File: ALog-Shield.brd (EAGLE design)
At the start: 53.3 x 78.5 mm, 32 parts

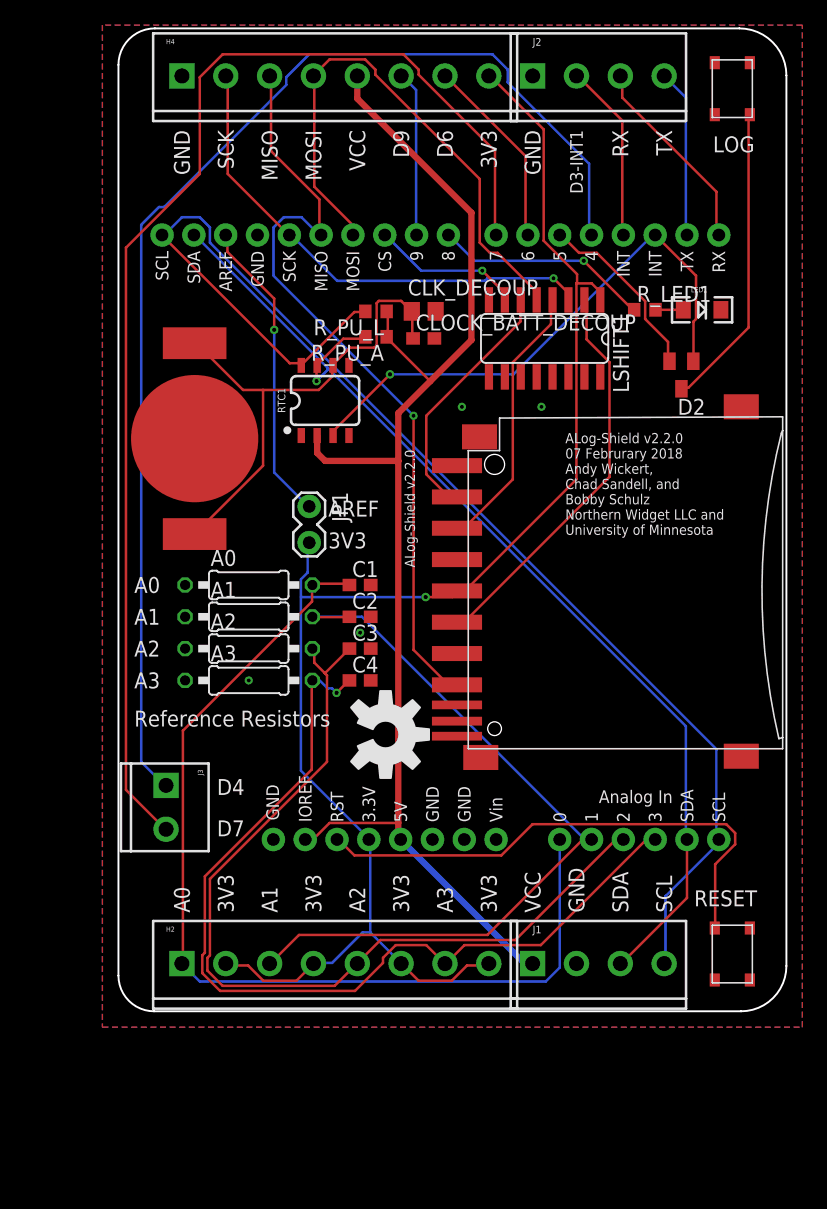
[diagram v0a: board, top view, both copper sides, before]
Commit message: IO Ref conversion
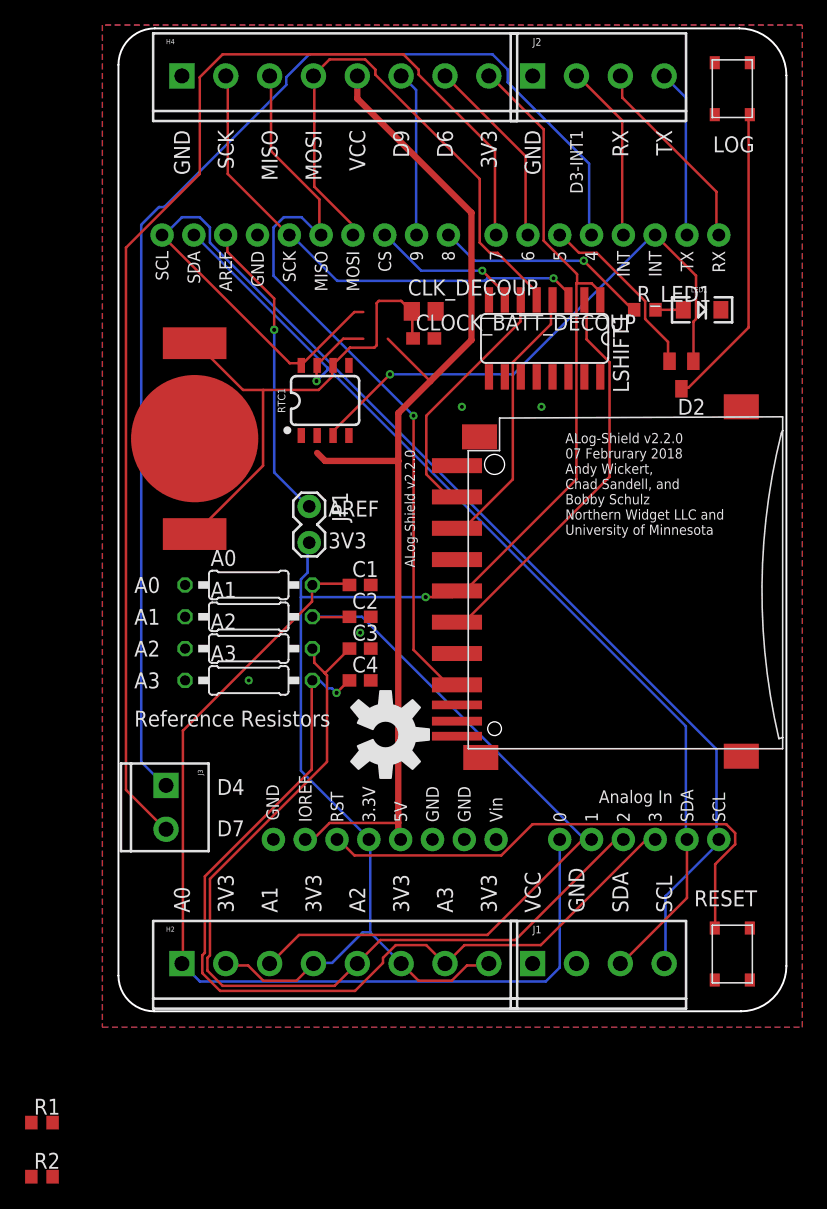
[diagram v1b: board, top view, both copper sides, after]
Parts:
- removed R_PU_A, R_PU_L: 10k, bschulz_passives:R0603
- added R1, R2: 10k, bschulz:R0603
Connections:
- new net 5V: U$9.5V
- net SCL: now also R1.1; no longer R_PU_L.2
- net SDA: now also R2.1; no longer R_PU_A.2
- net VCC: now also R1.2, R2.2; no longer R_PU_A.1, R_PU_L.1, U$9.5V
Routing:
- net VCC: track 105.4 -> 87.1 mm
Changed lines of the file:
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@@
 <?xml version="1.0" encoding="utf-8"?>
 <!DOCTYPE eagle SYSTEM "eagle.dtd">
-<eagle version="8.6.0">
+<eagle version="8.5.1">
 <drawing>
 <settings>
@@
 <layer number="20" name="Dimension" color="15" fill="1" visible="yes" active="yes"/>
 <layer number="21" name="tPlace" color="7" fill="1" visible="yes" active="yes"/>
-<layer number="22" name="bPlace" color="7" fill="1" visible="yes" active="yes"/>
+<layer number="22" name="bPlace" color="7" fill="1" visible="no" active="yes"/>
 <layer number="23" name="tOrigins" color="15" fill="1" visible="yes" active="yes"/>
 <layer number="24" name="bOrigins" color="15" fill="1" visible="yes" active="yes"/>
@@
 </element>
 <element name="JP1" library="SparkFun-Connectors" package="1X02_LOCK" value="" x="15.24" y="40.132" rot="R270"/>
-<element name="R_PU_L" library="bschulz_passives" package="R0603" value="10k" x="20.574" y="55.88" rot="R180">
-<attribute name="DIGIKEY" value="311-10.0KHRCT-ND" x="20.574" y="55.88" size="1.778" layer="27" rot="R180" display="off"/>
-<attribute name="MF" value="Yageo" x="20.574" y="55.88" size="1.778" layer="27" rot="R180" display="off"/>
-<attribute name="MPN" value="RC0603FR-0710KL" x="20.574" y="55.88" size="1.778" layer="27" rot="R180" display="off"/>
-<attribute name="VALUE_PART" value="10k" x="20.574" y="55.88" size="1.778" layer="27" rot="R180" display="off"/>
-</element>
-<element name="R_PU_A" library="bschulz_passives" package="R0603" value="10k" x="20.574" y="53.848" rot="R180">
-<attribute name="DIGIKEY" value="311-10.0KHRCT-ND" x="20.574" y="53.848" size="1.778" layer="27" rot="R180" display="off"/>
-<attribute name="MF" value="Yageo" x="20.574" y="53.848" size="1.778" layer="27" rot="R180" display="off"/>
-<attribute name="MPN" value="RC0603FR-0710KL" x="20.574" y="53.848" size="1.778" layer="27" rot="R180" display="off"/>
-<attribute name="VALUE_PART" value="10k" x="20.574" y="53.848" size="1.778" layer="27" rot="R180" display="off"/>
-</element>
 <element name="C1" library="bschulz_passives" package="C0603" value="" x="19.304" y="34.036">
 <attribute name="DIGIKEY" value="1276-1005-1-ND" x="19.304" y="34.036" size="1.778" layer="27" display="off"/>
@@
 <attribute name="MF" value="Maxim" x="16.51" y="48.768" size="1.778" layer="27" display="off"/>
 <attribute name="MPN" value="DS3231MZ+" x="16.51" y="48.768" size="1.778" layer="27" display="off"/>
+</element>
+<element name="R1" library="bschulz" package="R0603" value="10k" x="-6.096" y="-8.89">
+<attribute name="DIGIKEY" value="" x="-6.096" y="-8.89" size="1.778" layer="27" display="off"/>
+<attribute name="MF" value="" x="-6.096" y="-8.89" size="1.778" layer="27" display="off"/>
+<attribute name="MPN" value="" x="-6.096" y="-8.89" size="1.778" layer="27" display="off"/>
+<attribute name="VALUE_PART" value="" x="-6.096" y="-8.89" size="1.778" layer="27" display="off"/>
+</element>
+<element name="R2" library="bschulz" package="R0603" value="10k" x="-6.096" y="-13.208">
+<attribute name="DIGIKEY" value="" x="-6.096" y="-13.208" size="1.778" layer="27" display="off"/>
+<attribute name="MF" value="" x="-6.096" y="-13.208" size="1.778" layer="27" display="off"/>
+<attribute name="MPN" value="" x="-6.096" y="-13.208" size="1.778" layer="27" display="off"/>
+<attribute name="VALUE_PART" value="" x="-6.096" y="-13.208" size="1.778" layer="27" display="off"/>
 </element>
 </elements>
@@
 </signal>
 <signal name="VCC">
-<contactref element="U$9" pad="5V"/>
 <contactref element="J1" pad="1"/>
 <contactref element="H4" pad="5"/>
-<contactref element="U$9" pad="IOREF"/>
 <wire x1="19.08" y1="74.676" x2="19.08" y2="72.868" width="0.508" layer="1"/>
 <wire x1="19.08" y1="72.868" x2="28.194" y2="63.754" width="0.508" layer="1"/>
@@
 <wire x1="16.8656" y1="15.0368" x2="15.6464" y2="13.8176" width="0.2032" layer="1"/>
 <wire x1="22.352" y1="15.0368" x2="16.8656" y2="15.0368" width="0.2032" layer="1"/>
-<wire x1="15.0368" y1="13.8176" x2="14.9225" y2="13.716" width="0.2032" layer="1"/>
 <wire x1="22.352" y1="15.0368" x2="22.352" y2="13.9065" width="0.508" layer="1"/>
-<wire x1="22.352" y1="13.9065" x2="22.5425" y2="13.716" width="0.508" layer="1"/>
-<wire x1="22.5425" y1="13.716" x2="32.4485" y2="3.81" width="0.508" layer="16"/>
 <wire x1="32.4485" y1="3.81" x2="33.08" y2="3.81" width="0.508" layer="16"/>
-<contactref element="R_PU_L" pad="1"/>
-<contactref element="R_PU_A" pad="1"/>
-<wire x1="21.5138" y1="56.007" x2="21.424" y2="55.88" width="0.2032" layer="1"/>
+<wire x1="24.9047" y1="50.3047" x2="21.5138" y2="53.6956" width="0.2032" layer="1"/>
+<wire x1="16.51" y1="43.942" x2="15.875" y2="44.577" width="0.508" layer="1"/>
 <contactref element="RTC1" pad="2"/>
-<wire x1="21.5138" y1="55.8292" x2="21.5138" y2="53.8734" width="0.2032" layer="1"/>
-<wire x1="21.5138" y1="53.8734" x2="21.424" y2="53.848" width="0.2032" layer="1"/>
-<wire x1="21.5138" y1="55.8292" x2="21.424" y2="55.88" width="0.2032" layer="1"/>
-<wire x1="24.9047" y1="50.3047" x2="21.5138" y2="53.6956" width="0.2032" layer="1"/>
-<wire x1="21.5138" y1="53.6956" x2="21.424" y2="53.848" width="0.2032" layer="1"/>
 <wire x1="16.002" y1="45.8724" x2="15.875" y2="45.968" width="0.2032" layer="1"/>
-<wire x1="15.875" y1="44.577" x2="15.875" y2="45.968" width="0.508" layer="1"/>
-<wire x1="16.51" y1="43.942" x2="15.875" y2="44.577" width="0.508" layer="1"/>
+<contactref element="U$9" pad="IOREF"/>
+<contactref element="R1" pad="2"/>
+<contactref element="R2" pad="2"/>
+<wire x1="15.875" y1="44.577" x2="16.002" y2="45.8724" width="0" layer="19" extent="1-1"/>
+<wire x1="14.9225" y1="13.716" x2="15.0368" y2="13.8176" width="0" layer="19" extent="1-1"/>
+<wire x1="32.4485" y1="3.81" x2="22.352" y2="13.9065" width="0" layer="19" extent="1-16"/>
+<wire x1="-5.246" y1="-8.89" x2="14.9225" y2="13.716" width="0" layer="19" extent="1-1"/>
+<wire x1="-5.246" y1="-13.208" x2="-5.246" y2="-8.89" width="0" layer="19" extent="1-1"/>
 </signal>
 <signal name="DI">
@@
 <wire x1="47.752" y1="13.8176" x2="47.9425" y2="13.716" width="0.2032" layer="16"/>
 <wire x1="3.6576" y1="61.976" x2="3.4925" y2="61.976" width="0.2032" layer="16"/>
-<contactref element="R_PU_L" pad="2"/>
+<wire x1="13.6906" y1="51.7398" x2="14.5796" y2="51.7398" width="0.2032" layer="1"/>
+<wire x1="3.556" y1="61.8744" x2="13.6906" y2="51.7398" width="0.2032" layer="1"/>
+<wire x1="3.556" y1="61.8744" x2="3.4925" y2="61.976" width="0.2032" layer="1"/>
 <contactref element="RTC1" pad="8"/>
 <wire x1="18.8468" y1="55.8292" x2="19.558" y2="55.8292" width="0.2032" layer="1"/>
 <wire x1="14.7574" y1="51.7398" x2="18.8468" y2="55.8292" width="0.2032" layer="1"/>
-<wire x1="19.558" y1="55.8292" x2="19.724" y2="55.88" width="0.2032" layer="1"/>
 <wire x1="14.7574" y1="51.7398" x2="14.605" y2="51.568" width="0.2032" layer="1"/>
-<wire x1="13.6906" y1="51.7398" x2="14.5796" y2="51.7398" width="0.2032" layer="1"/>
-<wire x1="3.556" y1="61.8744" x2="13.6906" y2="51.7398" width="0.2032" layer="1"/>
-<wire x1="14.5796" y1="51.7398" x2="14.605" y2="51.568" width="0.2032" layer="1"/>
-<wire x1="3.556" y1="61.8744" x2="3.4925" y2="61.976" width="0.2032" layer="1"/>
+<contactref element="R1" pad="1"/>
+<wire x1="14.5796" y1="51.7398" x2="14.7574" y2="51.7398" width="0" layer="19" extent="1-1"/>
+<wire x1="-6.946" y1="-8.89" x2="43.58" y2="3.81" width="0" layer="19" extent="1-1"/>
 </signal>
 <signal name="SDA">
@@
 <wire x1="45.3136" y1="13.8176" x2="45.4025" y2="13.716" width="0.2032" layer="16"/>
 <wire x1="6.096" y1="61.976" x2="6.0325" y2="61.976" width="0.2032" layer="16"/>
-<contactref element="R_PU_A" pad="2"/>
+<wire x1="15.8242" y1="50.3174" x2="15.8242" y2="51.562" width="0.2032" layer="1"/>
+<wire x1="16.7132" y1="51.2064" x2="15.8242" y2="50.3174" width="0.2032" layer="16"/>
+<wire x1="16.7132" y1="51.3842" x2="16.7132" y2="51.2064" width="0.2032" layer="16"/>
+<wire x1="16.7132" y1="51.3842" x2="16.7005" y2="51.3715" width="0.2032" layer="16"/>
+<via x="15.8242" y="50.3174" extent="1-16" drill="0.3302"/>
 <contactref element="RTC1" pad="7"/>
 <wire x1="17.9578" y1="53.6956" x2="19.558" y2="53.6956" width="0.2032" layer="1"/>
 <wire x1="16.002" y1="51.7398" x2="17.9578" y2="53.6956" width="0.2032" layer="1"/>
-<wire x1="19.558" y1="53.6956" x2="19.724" y2="53.848" width="0.2032" layer="1"/>
 <wire x1="16.002" y1="51.7398" x2="15.875" y2="51.568" width="0.2032" layer="1"/>
-<wire x1="15.8242" y1="50.3174" x2="15.8242" y2="51.562" width="0.2032" layer="1"/>
-<wire x1="16.7132" y1="51.2064" x2="15.8242" y2="50.3174" width="0.2032" layer="16"/>
-<wire x1="16.7132" y1="51.3842" x2="16.7132" y2="51.2064" width="0.2032" layer="16"/>
-<wire x1="15.8242" y1="51.562" x2="15.875" y2="51.568" width="0.2032" layer="1"/>
-<wire x1="16.7132" y1="51.3842" x2="16.7005" y2="51.3715" width="0.2032" layer="16"/>
-<via x="15.8242" y="50.3174" extent="1-16" drill="0.3302"/>
+<contactref element="R2" pad="1"/>
+<wire x1="15.8242" y1="51.562" x2="15.875" y2="51.568" width="0" layer="19" extent="1-1"/>
+<wire x1="-6.946" y1="-13.208" x2="40.08" y2="3.81" width="0" layer="19" extent="1-1"/>
 </signal>
 <signal name="INT0">
@@
 <via x="12.446" y="54.4068" extent="1-16" drill="0.3302"/>
 </signal>
+<signal name="5V">
+<contactref element="U$9" pad="5V"/>
+</signal>
 </signals>

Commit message: PU, reroute, 5V terminal
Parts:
- removed J3: (no value), SparkFun-Connectors:SCREWTERMINAL-3.5MM-2
- added JP2: (no value), SparkFun-Connectors:SCREWTERMINAL-3.5MM-3
- moved R2 71.8 mm to (19.6, 53.8), turned to 180 degrees
- moved R1 69.7 mm to (19.6, 55.9)
- moved CLK_DECOUP 0.57 mm to (23.9, 56.1)
- moved CLOCK_BATT_DECOUP 0.51 mm to (23.9, 53.7)
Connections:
- net 5V: now also JP2.3
- net D4: now also JP2.1; no longer J3.1
- net D7: now also JP2.2; no longer J3.2
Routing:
- net VCC: track 87.1 -> 114.7 mm, vias 0 -> 1
- net 5V: track 0.00 -> 20.5 mm, vias 0 -> 1
- net D4: track 97.5 -> 85.0 mm
- net D7: track 98.4 -> 91.6 mm
- net BAT: track 40.8 -> 37.4 mm
- net SDA: track 84.0 -> 85.0 mm
- net SCL: track 104.3 -> 103.4 mm
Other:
- board text added: "5V"

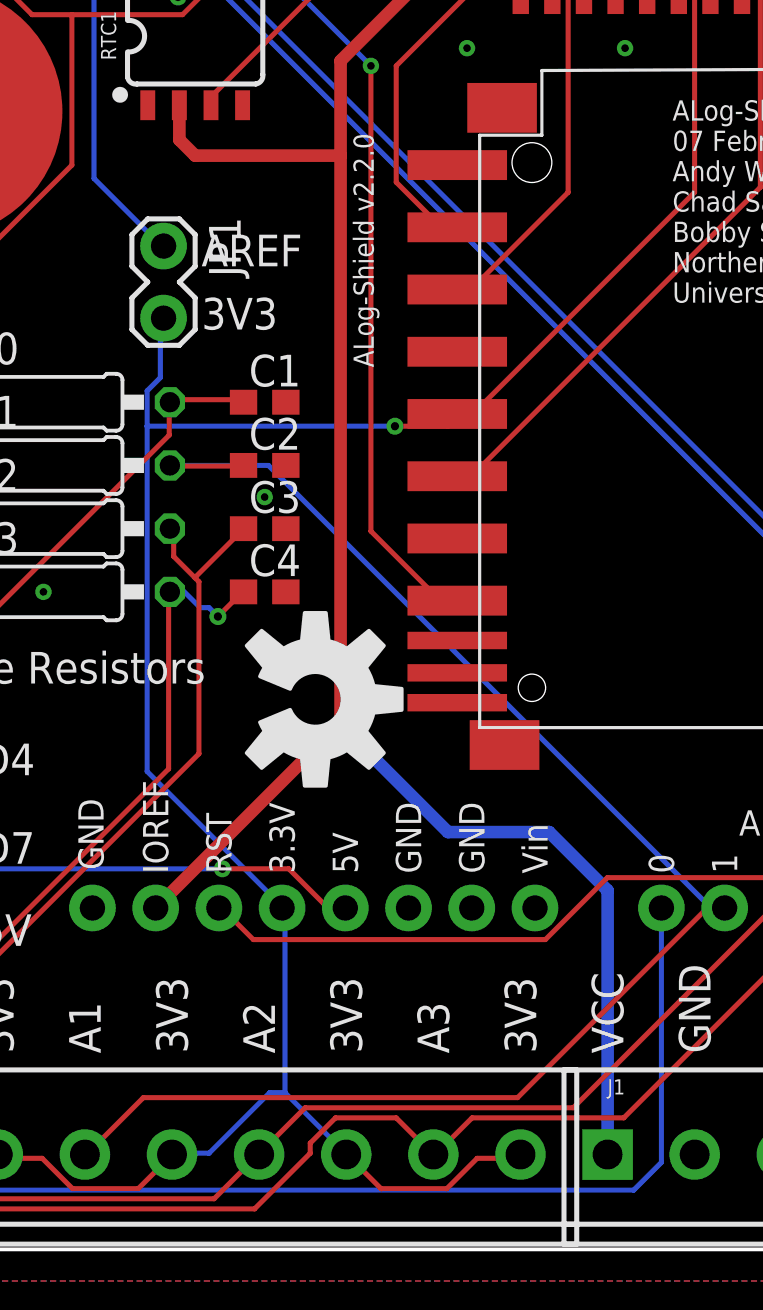
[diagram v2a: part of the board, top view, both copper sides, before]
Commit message: Larger via
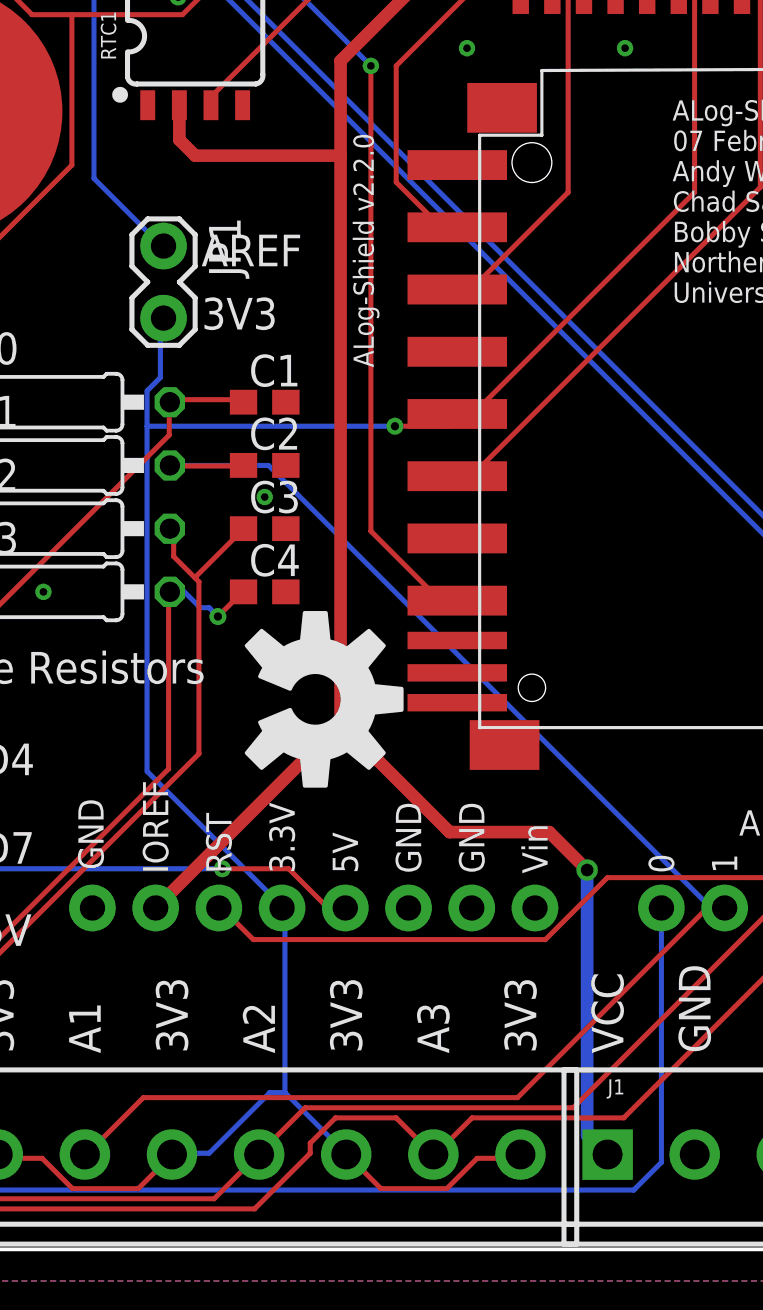
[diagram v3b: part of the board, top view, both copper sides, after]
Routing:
- net VCC: track 114.7 -> 113.9 mm
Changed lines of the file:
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@@
 <wire x1="28.194" y1="57.2516" x2="28.194" y2="53.594" width="0.508" layer="1"/>
 <wire x1="22.352" y1="43.942" x2="16.51" y2="43.942" width="0.508" layer="1"/>
-<wire x1="32.4485" y1="3.81" x2="33.08" y2="3.81" width="0.508" layer="16"/>
 <wire x1="16.51" y1="43.942" x2="15.875" y2="44.577" width="0.508" layer="1"/>
 <contactref element="RTC1" pad="2"/>
@@
 <contactref element="R2" pad="2"/>
 <wire x1="15.875" y1="44.577" x2="15.875" y2="45.968" width="0.508" layer="1"/>
-<wire x1="14.9225" y1="13.716" x2="22.20595" y2="20.99945" width="0.508" layer="1"/>
-<wire x1="22.20595" y1="20.99945" x2="22.352" y2="21.1455" width="0.508" layer="1"/>
-<wire x1="22.352" y1="21.1455" x2="22.352" y2="43.942" width="0.508" layer="1"/>
-<wire x1="33.08" y1="3.81" x2="33.08" y2="14.418" width="0.508" layer="16"/>
-<wire x1="33.08" y1="14.418" x2="30.734" y2="16.764" width="0.508" layer="16"/>
-<wire x1="30.734" y1="16.764" x2="26.67" y2="16.764" width="0.508" layer="16"/>
-<wire x1="26.67" y1="16.764" x2="22.352" y2="21.082" width="0.508" layer="16"/>
-<via x="22.352" y="21.082" extent="1-16" drill="0.3302"/>
+<wire x1="22.352" y1="43.942" x2="22.352" y2="21.1455" width="0.508" layer="1"/>
 <wire x1="18.8468" y1="54.4068" x2="18.8468" y2="53.8734" width="0.2032" layer="1"/>
 <wire x1="20.2692" y1="55.8292" x2="18.8468" y2="54.4068" width="0.2032" layer="1"/>
@@
 <wire x1="28.194" y1="57.2516" x2="22.225" y2="57.2516" width="0.2032" layer="1"/>
 <wire x1="20.447" y1="56.007" x2="20.408" y2="55.88" width="0.2032" layer="1"/>
-<wire x1="22.225" y1="20.9804" x2="22.20595" y2="20.99945" width="0.2032" layer="1"/>
-<wire x1="22.225" y1="20.9804" x2="22.352" y2="21.082" width="0.2032" layer="1"/>
+<wire x1="22.352" y1="21.1455" x2="14.9225" y2="13.716" width="0.508" layer="1"/>
+<wire x1="22.352" y1="21.1455" x2="26.7335" y2="16.764" width="0.508" layer="1"/>
+<wire x1="26.7335" y1="16.764" x2="30.734" y2="16.764" width="0.508" layer="1"/>
+<wire x1="32.258" y1="15.24" x2="30.734" y2="16.764" width="0.508" layer="1"/>
+<wire x1="32.258" y1="4.572" x2="32.258" y2="15.24" width="0.508" layer="16"/>
+<wire x1="33.02" y1="3.81" x2="32.258" y2="4.572" width="0.508" layer="16"/>
+<wire x1="33.02" y1="3.81" x2="33.08" y2="3.81" width="0.508" layer="16"/>
+<via x="32.258" y="15.24" extent="1-16" drill="0.508"/>
 </signal>
 <signal name="DI">
